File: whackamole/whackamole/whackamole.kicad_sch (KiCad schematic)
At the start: 20 parts

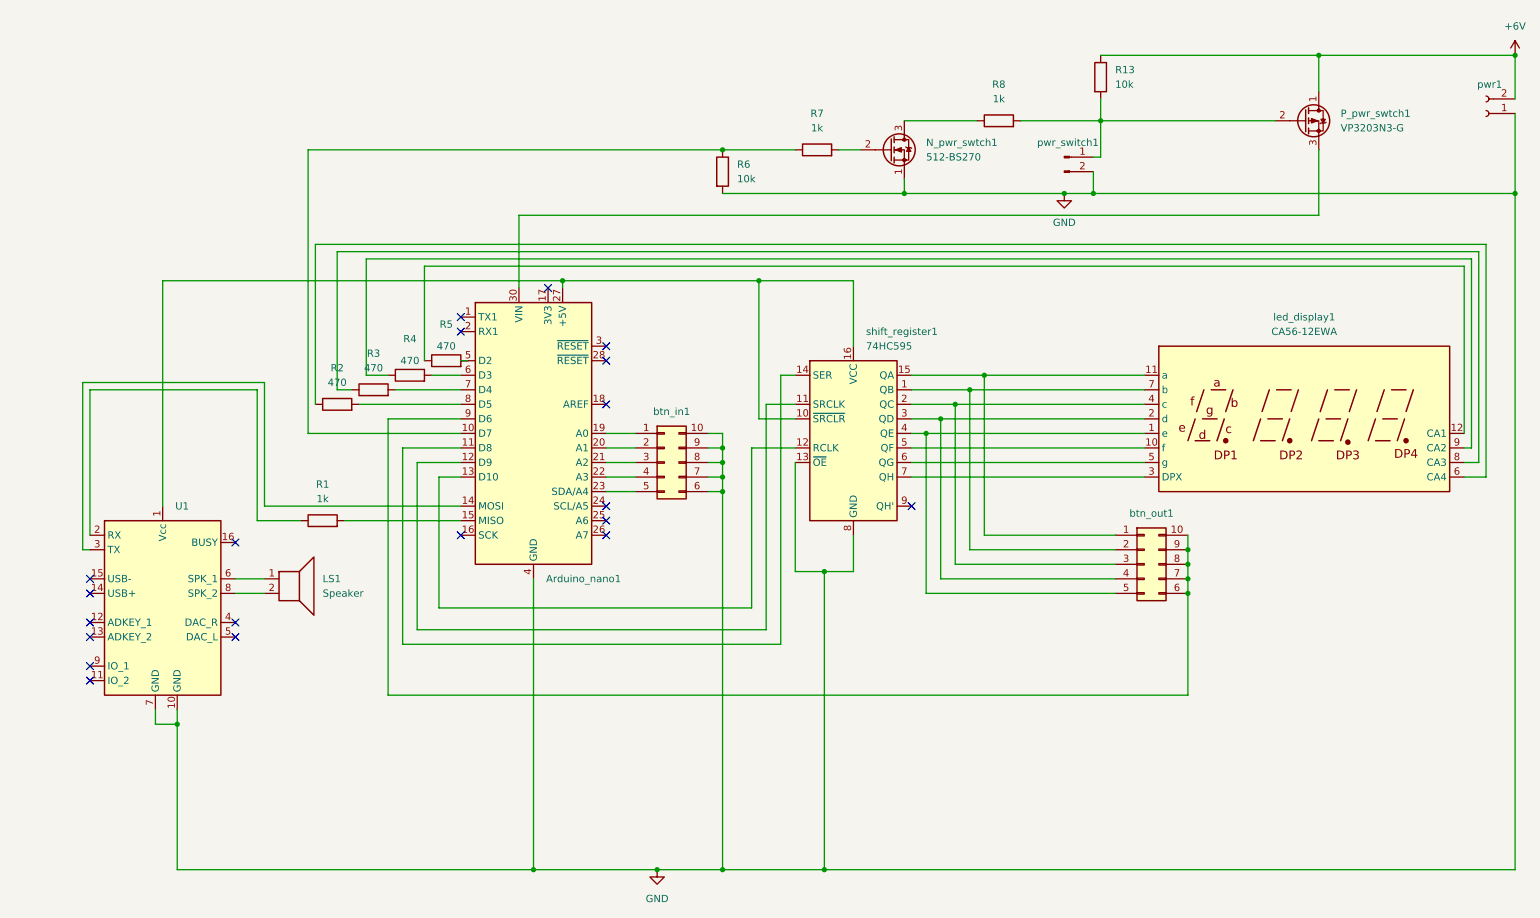
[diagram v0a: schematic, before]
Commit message: capacitor to regulate player tension and avoid unexpected shutdowns
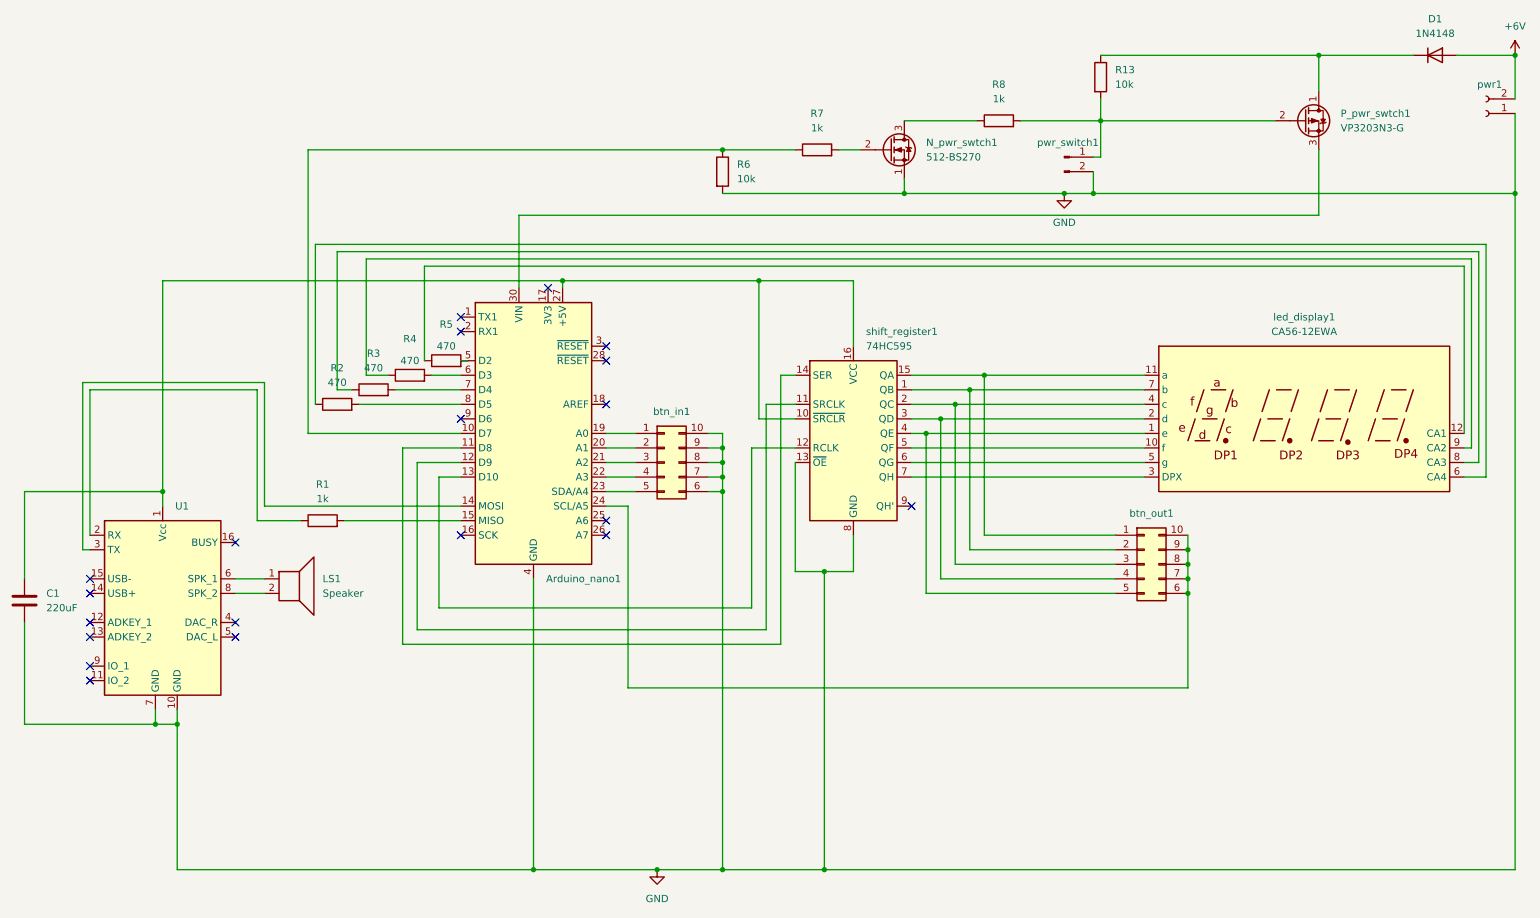
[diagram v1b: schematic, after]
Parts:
- added C1: 220uF, symbol Device:C
- added D1: 1N4148, Diode_THT:D_DO-35_SOD27_P7.62mm_Horizontal, symbol Diode:1N4148
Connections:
- net +6V: now also D1.2 (A); no longer P_pwr_swtch1.1 (D), R13.1
- net GND: now also C1.2
- net at Arduino_nano1.24 (SCL/A5): now also btn_out1.10 (Pin_10), btn_out1.6 (Pin_6), btn_out1.7 (Pin_7), btn_out1.8 (Pin_8), btn_out1.9 (Pin_9)
- net at Arduino_nano1.27 (+5V), U1.1 (Vcc), shift_register1.10 (~{SRCLR})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: now also C1.1
- new net: D1.1 (K), P_pwr_swtch1.1 (D), R13.1
- now unconnected: Arduino_nano1.9 (D6)
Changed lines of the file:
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@@
   (junction (at 140.97 88.9) (diameter 0) (color 0 0 0 0)
   )
+  (junction (at 43.18 96.52) (diameter 0) (color 0 0 0 0)
+  )
   (junction (at 181.61 81.28) (diameter 0) (color 0 0 0 0)
   )
@@
   (junction (at 113.03 59.69) (diameter 0) (color 0 0 0 0)
   )
+  (junction (at 41.91 137.16) (diameter 0) (color 0 0 0 0)
+  )
   (junction (at 245.11 20.32) (diameter 0) (color 0 0 0 0)
   )
@@
   (junction (at 279.4 44.45) (diameter 0) (color 0 0 0 0)
   )
-  (no_connect (at 120.65 99.06))
   (no_connect (at 55.88 119.38))
   (no_connect (at 30.48 129.54))
@@
   (no_connect (at 30.48 127))
   (no_connect (at 120.65 71.12))
+  (no_connect (at 95.25 83.82))
   (no_connect (at 120.65 81.28))
   (no_connect (at 120.65 101.6))
@@
   (no_connect (at 30.48 119.38))
   (no_connect (at 30.48 111.76))
+  (wire (pts (xy 19.05 137.16) (xy 41.91 137.16))
+    (stroke (width 0) (type default))
+  )
   (wire (pts (xy 120.65 91.44) (xy 125.73 91.44))
     (stroke (width 0) (type default))
@@
     (stroke (width 0) (type default))
   )
+  (wire (pts (xy 19.05 119.38) (xy 19.05 137.16))
+    (stroke (width 0) (type default))
+  )
+  (wire (pts (xy 43.18 96.52) (xy 43.18 59.69))
+    (stroke (width 0) (type default))
+  )
   (wire (pts (xy 193.04 31.75) (xy 207.01 31.75))
     (stroke (width 0) (type default))
@@
     (stroke (width 0) (type default))
   )
+  (wire (pts (xy 19.05 96.52) (xy 43.18 96.52))
+    (stroke (width 0) (type default))
+  )
   (wire (pts (xy 78.74 76.2) (xy 82.55 76.2))
     (stroke (width 0) (type default))
@@
     (stroke (width 0) (type default))
   )
+  (wire (pts (xy 222.25 130.81) (xy 124.46 130.81))
+    (stroke (width 0) (type default))
+  )
   (wire (pts (xy 222.25 104.14) (xy 222.25 106.68))
     (stroke (width 0) (type default))
@@
     (stroke (width 0) (type default))
   )
-  (wire (pts (xy 82.55 83.82) (xy 95.25 83.82))
-    (stroke (width 0) (type default))
-  )
   (wire (pts (xy 148.59 120.65) (xy 87.63 120.65))
     (stroke (width 0) (type default))
   )
-  (wire (pts (xy 43.18 99.06) (xy 43.18 59.69))
+  (wire (pts (xy 43.18 99.06) (xy 43.18 96.52))
     (stroke (width 0) (type default))
   )
@@
     (stroke (width 0) (type default))
   )
-  (wire (pts (xy 82.55 132.08) (xy 82.55 83.82))
+  (wire (pts (xy 41.91 137.16) (xy 45.72 137.16))
     (stroke (width 0) (type default))
   )
@@
     (stroke (width 0) (type default))
   )
-  (wire (pts (xy 82.55 132.08) (xy 222.25 132.08))
-    (stroke (width 0) (type default))
-  )
   (wire (pts (xy 85.09 88.9) (xy 95.25 88.9))
     (stroke (width 0) (type default))
@@
     (stroke (width 0) (type default))
   )
+  (wire (pts (xy 124.46 99.06) (xy 120.65 99.06))
+    (stroke (width 0) (type default))
+  )
   (wire (pts (xy 172.72 44.45) (xy 200.66 44.45))
     (stroke (width 0) (type default))
@@
     (stroke (width 0) (type default))
   )
+  (wire (pts (xy 269.24 20.32) (xy 279.4 20.32))
+    (stroke (width 0) (type default))
+  )
   (wire (pts (xy 120.65 86.36) (xy 125.73 86.36))
     (stroke (width 0) (type default))
@@
     (stroke (width 0) (type default))
   )
-  (wire (pts (xy 245.11 20.32) (xy 279.4 20.32))
+  (wire (pts (xy 245.11 20.32) (xy 261.62 20.32))
     (stroke (width 0) (type default))
   )
@@
     (stroke (width 0) (type default))
   )
+  (wire (pts (xy 19.05 111.76) (xy 19.05 96.52))
+    (stroke (width 0) (type default))
+  )
   (wire (pts (xy 91.44 116.84) (xy 91.44 93.98))
     (stroke (width 0) (type default))
@@
     (stroke (width 0) (type default))
   )
+  (wire (pts (xy 124.46 130.81) (xy 124.46 99.06))
+    (stroke (width 0) (type default))
+  )
   (wire (pts (xy 153.67 83.82) (xy 147.32 83.82))
     (stroke (width 0) (type default))
@@
     (stroke (width 0) (type default))
   )
+  (wire (pts (xy 222.25 130.81) (xy 222.25 114.3))
+    (stroke (width 0) (type default))
+  )
   (wire (pts (xy 245.11 48.26) (xy 245.11 36.83))
     (stroke (width 0) (type default))
@@
     (stroke (width 0) (type default))
   )
-  (wire (pts (xy 41.91 137.16) (xy 45.72 137.16))
-    (stroke (width 0) (type default))
-  )
   (wire (pts (xy 45.72 162.56) (xy 107.95 162.56))
     (stroke (width 0) (type default))
@@
     (stroke (width 0) (type default))
   )
-  (wire (pts (xy 222.25 114.3) (xy 222.25 132.08))
-    (stroke (width 0) (type default))
-  )
   (wire (pts (xy 96.52 73.66) (xy 95.25 73.66))
     (stroke (width 0) (type default))
@@
   (wire (pts (xy 153.67 88.9) (xy 146.05 88.9))
     (stroke (width 0) (type default))
+  )
+  (symbol (lib_id "Diode:1N4148") (at 265.43 20.32 0) (unit 1)
+    (in_bom yes) (on_board yes) (dnp no) (fields_autoplaced)
+    (property "Reference" "D1" (at 265.43 13.97 0)
+      (effects (font (size 1.27 1.27)))
+    )
+    (property "Value" "1N4148" (at 265.43 16.51 0)
+      (effects (font (size 1.27 1.27)))
+    )
+    (property "Footprint" "Diode_THT:D_DO-35_SOD27_P7.62mm_Horizontal" (at 265.43 20.32 0)
+      (effects (font (size 1.27 1.27)) hide)
+    )
+    (property "Datasheet" "https://assets.nexperia.com/documents/data-sheet/1N4148_1N4448.pdf" (at 265.43 20.32 0)
+      (effects (font (size 1.27 1.27)) hide)
+    )
+    (property "Sim.Device" "D" (at 265.43 20.32 0)
+      (effects (font (size 1.27 1.27)) hide)
+    )
+    (property "Sim.Pins" "1=K 2=A" (at 265.43 20.32 0)
+      (effects (font (size 1.27 1.27)) hide)
+    )
+    (pin "2")
+    (pin "1")
+    (instances
+      (project "whackamole"
+        (path "/c1d152d8-520f-4b1f-be58-40784473a3d2"
+          (reference "D1") (unit 1)
+        )
+      )
+    )
   )
   (symbol (lib_id "MCU_Module:Arduino_Nano_Every") (at 107.95 86.36 0) (unit 1)
@@
         )
       )
+    )
+  )
+  (symbol (lib_id "Device:C") (at 19.05 115.57 0) (unit 1)
+    (in_bom yes) (on_board yes) (dnp no) (fields_autoplaced)
+    (property "Reference" "C1" (at 22.86 114.3 0)
+      (effects (font (size 1.27 1.27)) (justify left))
+    )
+    (property "Value" "220uF" (at 22.86 116.84 0)
+      (effects (font (size 1.27 1.27)) (justify left))
+    )
+    (property "Footprint" "" (at 20.0152 119.38 0)
+      (effects (font (size 1.27 1.27)) hide)
+    )
+    (property "Datasheet" "~" (at 19.05 115.57 0)
+      (effects (font (size 1.27 1.27)) hide)
+    )
+    (pin "2")
+    (pin "1")
+    (instances
+      (project "whackamole"
+        (path "/c1d152d8-520f-4b1f-be58-40784473a3d2"
+          (reference "C1") (unit 1)
+        )
+      )
